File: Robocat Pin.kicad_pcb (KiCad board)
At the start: 4 copper layers, 62.9 x 62.9 mm, 20 parts, among them SW1 SW_DP3T, U1 NA555P

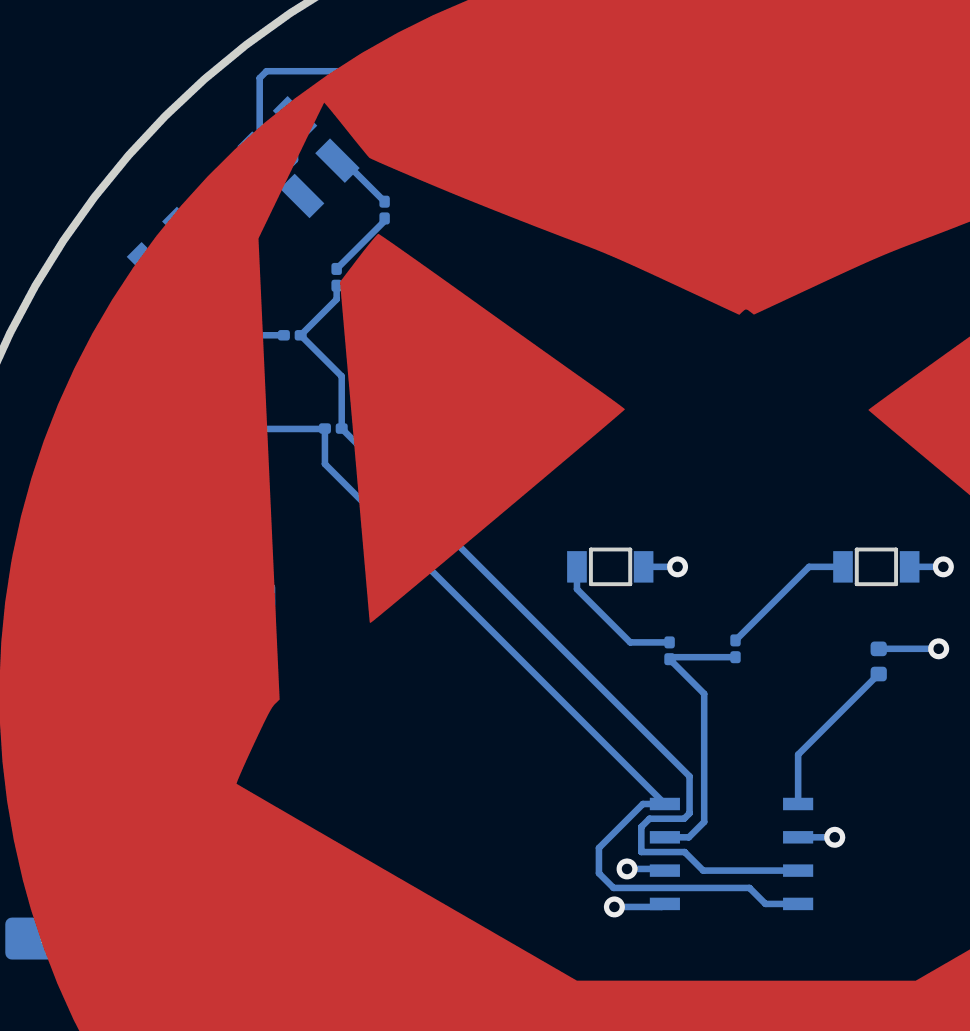
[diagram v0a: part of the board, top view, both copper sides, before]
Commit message: Worked on bom, working on redoing footprints for missing parts
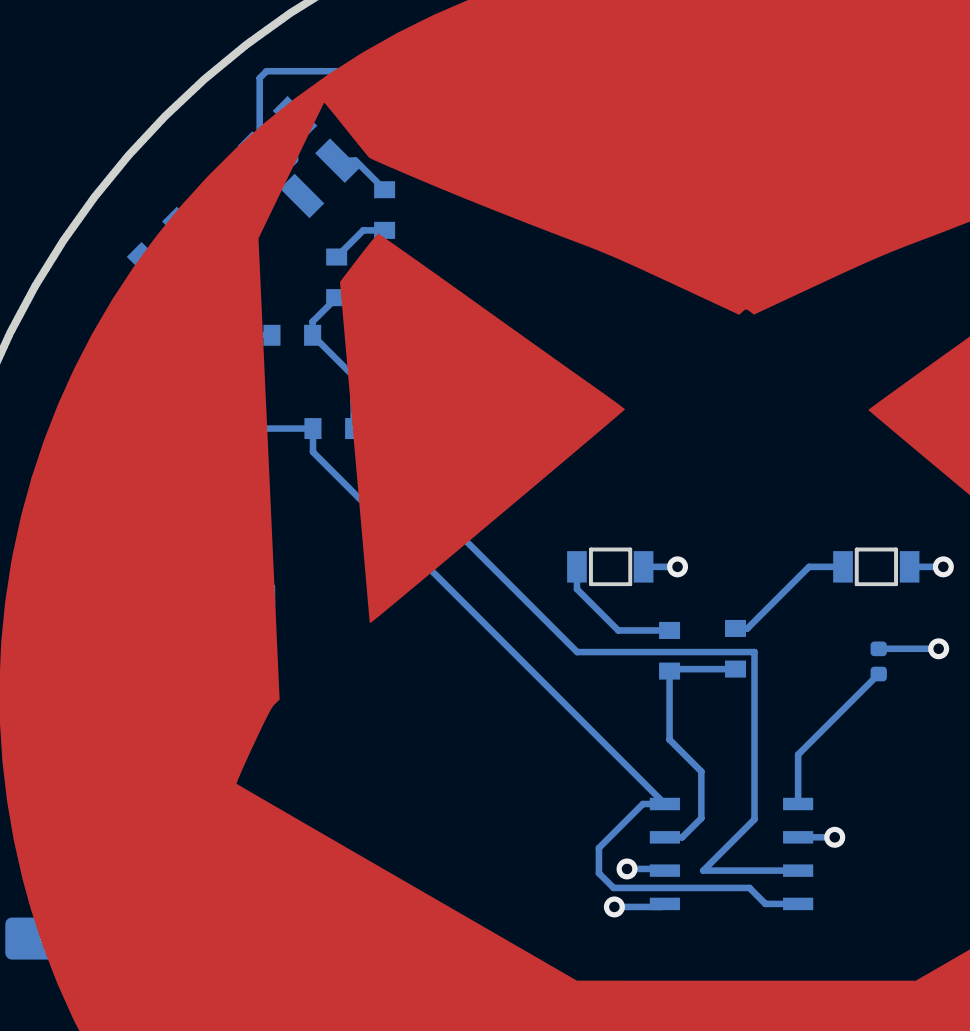
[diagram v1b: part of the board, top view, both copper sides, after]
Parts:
- BT1: value Battery_Cell -> Cell Battery
- D1, D2: value BLUE -> Blue LED
- R1, R2, R3, R4, R5, R6: footprint Resistor_SMD:R_0201_0603Metric -> Custom Library:0603 Resistor
- SW1: value SW_DP3T -> DP3T Switch
- U1: value NA555P -> 555 Integrated Circuit
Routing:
- net Net-(R1-Pad2): track 36.1 -> 37.6 mm
- net Net-(R5-Pad1): track 11.0 -> 10.4 mm

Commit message: Continued working on fixing footprints
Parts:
- added REF**: Pin Back, Custom Library:Pin Back, B.Cu at (52.7, 36.2)
- U1: footprint Custom Library:LM555CM -> Custom Library:SOIC - 8 555
- turned U1 to 0 degrees
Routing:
- net Net-(R1-Pad2): track 37.6 -> 34.2 mm

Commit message: Fixed footprints, parts, pcb
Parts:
- D1, D2: footprint Custom Library:1.3x3.2mm LED -> Custom Library:1206 LED
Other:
- outline, holes or cut-outs redrawn

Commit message: Fixed vias
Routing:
- net /gnd: track 116.1 -> 256.1 mm
- net Net-(C2-Pad1): track 111.9 -> 208.9 mm
- net (no net): vias 0 -> 1

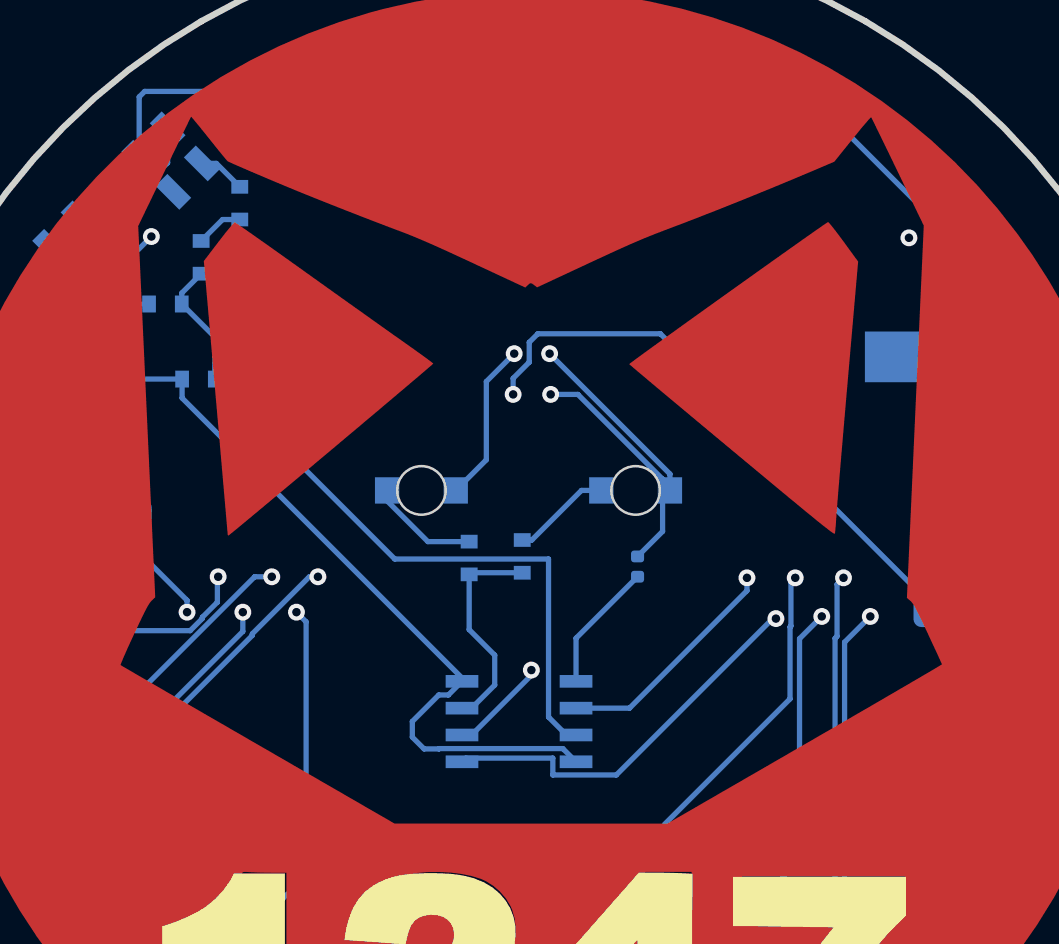
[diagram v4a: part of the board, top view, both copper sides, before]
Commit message: Fixed the robocat and pin back areas
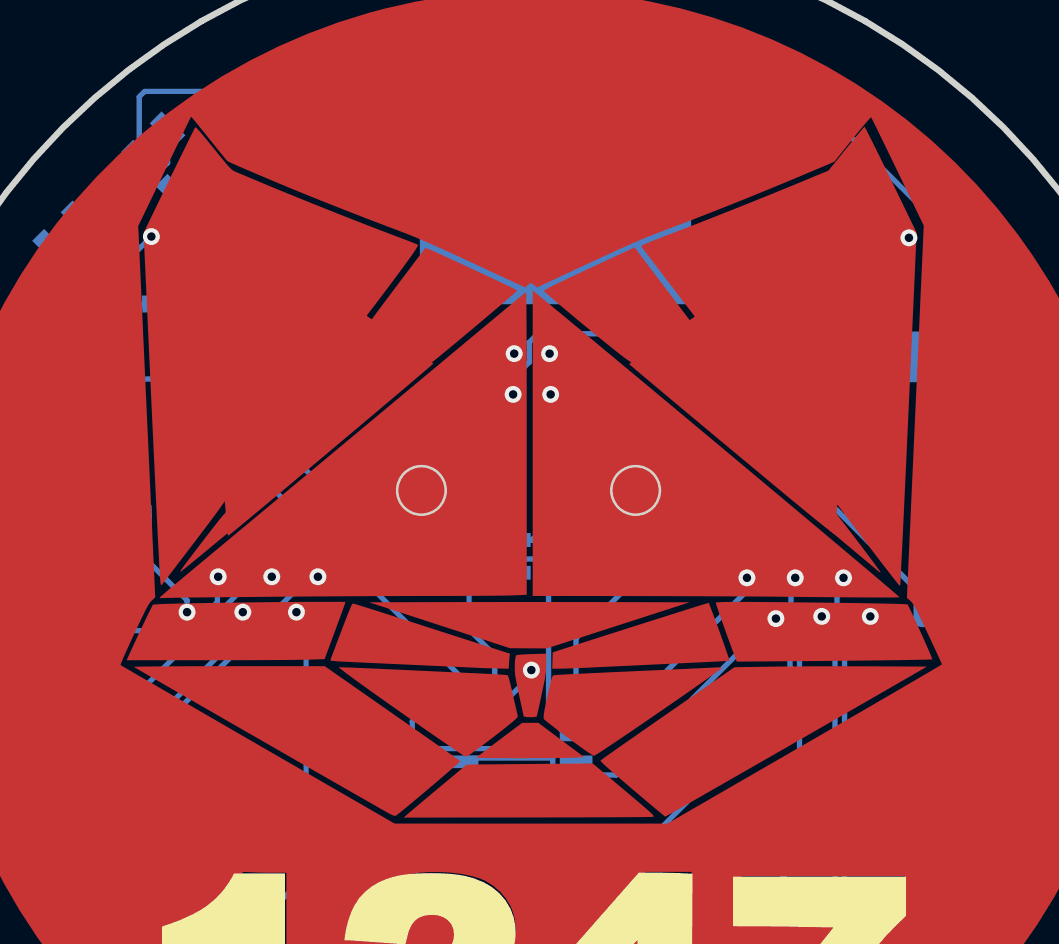
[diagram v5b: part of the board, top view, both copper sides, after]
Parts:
- added G***: Face, Robocat:Face, F.Cu at (52.8, 46.6)

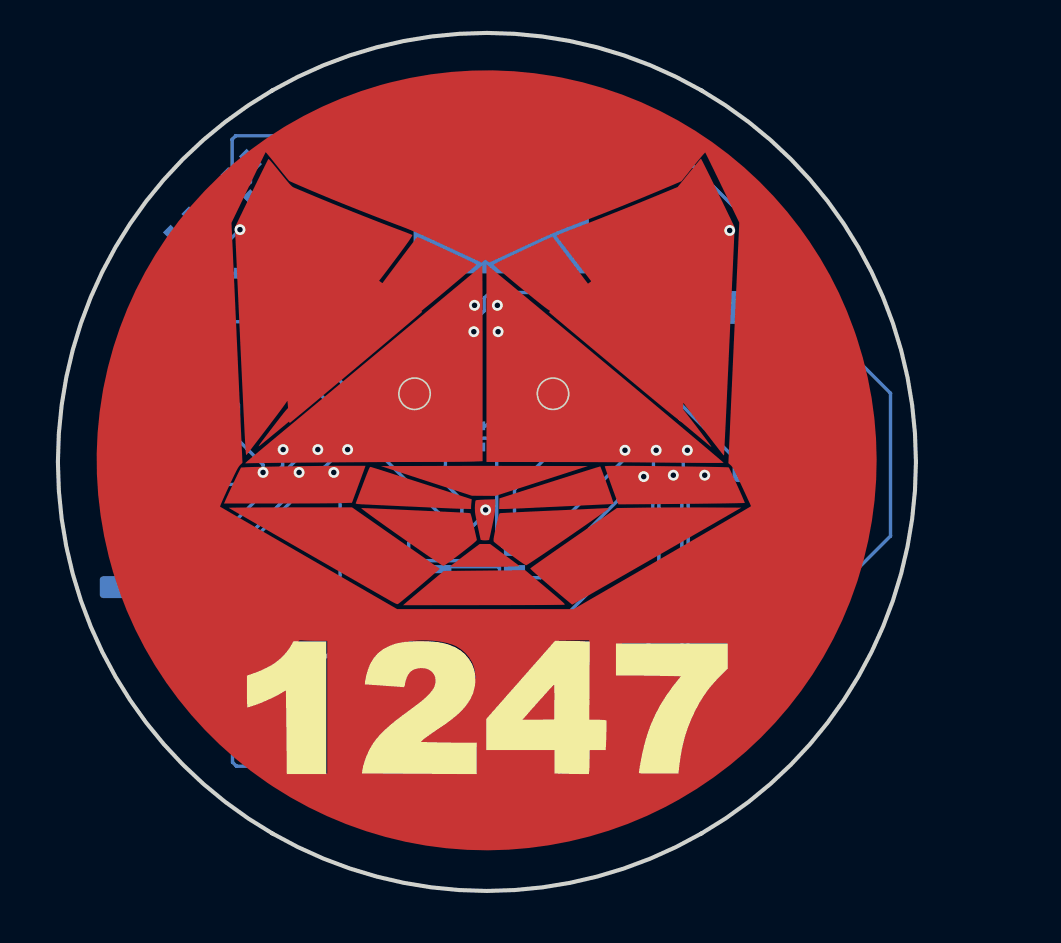
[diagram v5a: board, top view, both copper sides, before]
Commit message: Fixed issue that prevented it from blinking, cleaned up PCB design
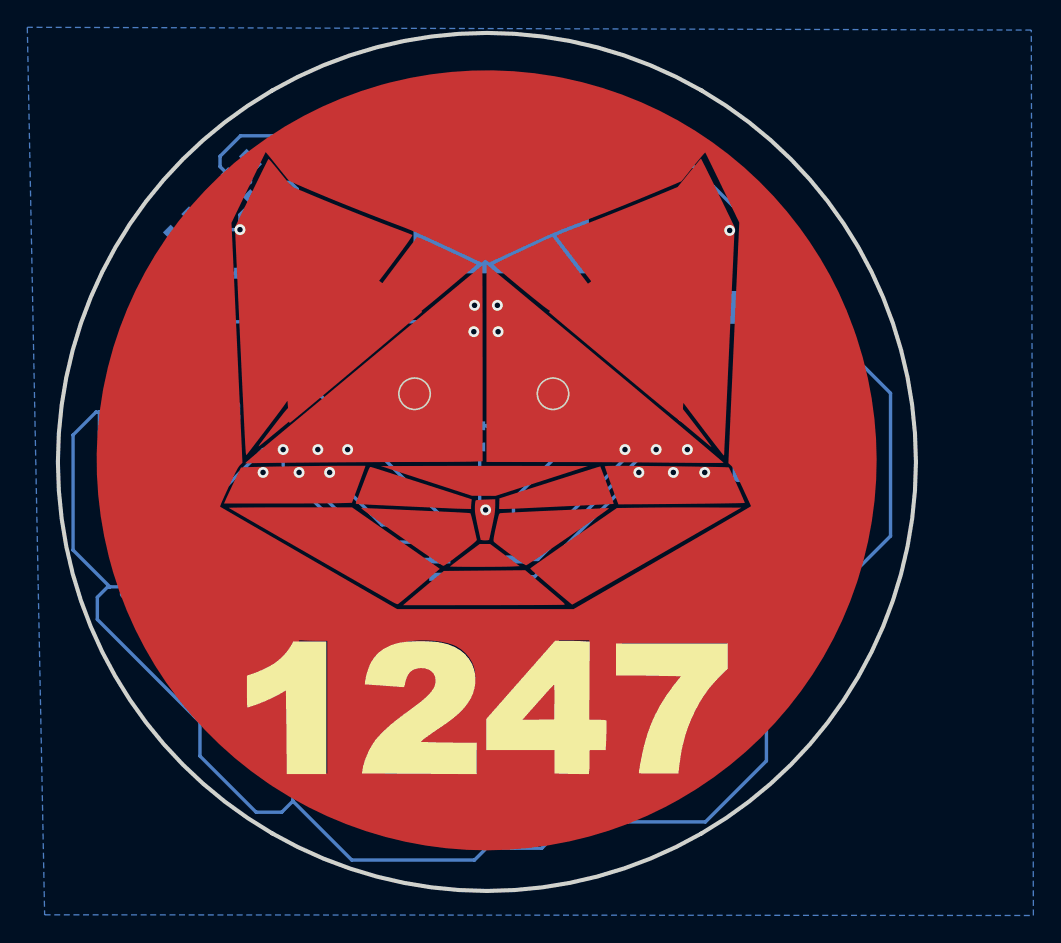
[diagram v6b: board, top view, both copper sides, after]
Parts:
- moved C5 1.47 mm to (30.6, 61.8)
- moved U1 0.56 mm to (52.2, 59.1)
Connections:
- C2 pad 1: Net-(C2-Pad1) -> Net-(U1-THR)
- C3 pad 1: Net-(C2-Pad1) -> Net-(U1-THR)
- C4 pad 1: Net-(C2-Pad1) -> Net-(U1-THR)
- C5 pad 1: Net-(C2-Pad1) -> Net-(U1-THR)
- C6 pad 1: Net-(C2-Pad1) -> Net-(U1-THR)
- SW1 pad 6: unconnected-(SW1-Pad6) -> Net-(U1-THR)
- SW1 pad 7: Net-(C2-Pad1) -> Net-(U1-THR)
- U1 pad 2: Net-(C2-Pad1) -> Net-(U1-THR)
- U1 pad 6: Net-(C2-Pad1) -> Net-(U1-THR)
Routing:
- net /gnd: track 256.1 -> 0.74 mm, vias 10 -> 8
- net Net-(C2-Pad1): track 208.9 -> 0.00 mm, vias 8 -> 0
- net Net-(U1-THR): track 0.00 -> 191.2 mm, vias 0 -> 5
- net Net-(#FLG01-pwr): track 51.2 -> 87.5 mm, vias 0 -> 2
- net Net-(U1-Q): track 10.1 -> 35.2 mm, vias 0 -> 2
- net Net-(U1-DIS): track 34.5 -> 51.2 mm, vias 0 -> 2
- net Net-(U1-CV): track 6.16 -> 6.75 mm
- net Net-(BT1-+): track 87.7 -> 88.2 mm
- net (no net): vias 1 -> 0
- added copper zone on B.Cu, net /gnd
- added copper zone on In2.Cu, net /gnd
